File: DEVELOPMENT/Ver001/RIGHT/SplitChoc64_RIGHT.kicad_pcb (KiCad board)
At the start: 2 copper layers, 177.6 x 96.8 mm, 80 parts, among them J2 BM02B-SRSS-TB, J4 3V3 GND X Y SW SDA SCL, U2 XIAO nRF52840 Plus

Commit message: Stage parallel trackball FFC connectors in Ver001
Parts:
- added J6: FH19C-6S-0.5SH(10), SplitChoc64_FFC:FH19C-6S-0.5SH_HandSolder, B.Cu at (194.7, 112.0)
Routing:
- net R_GND: track 193.8 -> 198.8 mm, vias 2 -> 3
- net R_JOY_X: track 167.7 -> 172.4 mm, vias 1 -> 2
- net R_JOY_Y: track 170.1 -> 171.1 mm, vias 1 -> 2
- net R_3V3: track 157.5 -> 158.1 mm, vias 2 -> 3
- net R_JOY_SW: track 165.4 -> 165.9 mm, vias 1 -> 2
- net R_JOY_SDA: track 165.7 -> 166.0 mm, vias 1 -> 2

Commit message: Repair parallel FFC fanout and publish DRC pass 2
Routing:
- net R_3V3: track 158.1 -> 179.2 mm, vias 3 -> 2
- net R_JOY_Y: track 171.1 -> 182.5 mm, vias 2 -> 1
- net R_JOY_SW: track 165.9 -> 177.0 mm, vias 2 -> 1
- net R_JOY_SDA: track 166.0 -> 176.5 mm, vias 2 -> 1
- net R_GND: track 198.8 -> 207.7 mm, vias 3 -> 2
- net R_JOY_X: track 172.4 -> 180.9 mm, vias 2 -> 1
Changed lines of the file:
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@@
 	(segment
 		(start 198.95 115.05)
-		(end 198.0 110.0949)
+		(end 185.073 116.0)
 		(width 0.15)
 		(layer "B.Cu")
 		(net 14)
 	)
-	(via
-		(at 198.0 110.0949)
-		(size 0.45)
-		(drill 0.2)
-		(layers "F.Cu" "B.Cu")
-		(net 14)
-	)
 	(segment
 		(start 199.45 115.05)
-		(end 198.8 110.3966)
+		(end 186.343 116.0)
 		(width 0.15)
 		(layer "B.Cu")
 		(net 16)
 	)
-	(via
-		(at 198.8 110.3966)
-		(size 0.45)
-		(drill 0.2)
-		(layers "F.Cu" "B.Cu")
-		(net 16)
-	)
 	(segment
 		(start 199.95 115.05)
-		(end 199.8 114.3)
+		(end 187.613 116.0)
 		(width 0.15)
 		(layer "B.Cu")
 		(net 17)
 	)
-	(via
-		(at 199.8 114.3)
-		(size 0.45)
-		(drill 0.2)
-		(layers "F.Cu" "B.Cu")
-		(net 17)
-	)
 	(segment
 		(start 200.45 115.05)
-		(end 200.4 114.72)
+		(end 188.883 116.0)
 		(width 0.15)
 		(layer "B.Cu")
 		(net 18)
 	)
-	(via
-		(at 200.4 114.72)
-		(size 0.45)
-		(drill 0.2)
-		(layers "F.Cu" "B.Cu")
-		(net 18)
-	)
 	(segment
 		(start 200.95 115.05)
-		(end 201.0 114.98)
+		(end 190.153 116.0)
 		(width 0.15)
 		(layer "B.Cu")
 		(net 19)
 	)
-	(via
-		(at 201.0 114.98)
-		(size 0.45)
-		(drill 0.2)
-		(layers "F.Cu" "B.Cu")
-		(net 19)
-	)
 	(segment
 		(start 201.45 115.05)
-		(end 201.6 115.4)
+		(end 201.45 113.5)
 		(width 0.15)
 		(layer "B.Cu")
 		(net 21)
 	)
-	(via
-		(at 201.6 115.4)
-		(size 0.45)
-		(drill 0.2)
-		(layers "F.Cu" "B.Cu")
+	(segment
+		(start 201.45 113.5)
+		(end 183.803 113.5)
+		(width 0.15)
+		(layer "B.Cu")
 		(net 21)
 	)
 	(segment
-		(start 199.8 114.3)
-		(end 199.8 114.5693)
+		(start 183.803 113.5)
+		(end 183.803 116.0)
 		(width 0.15)
-		(layer "F.Cu")
-		(net 17)
-	)
-	(segment
-		(start 200.4 114.72)
-		(end 200.4 114.871)
-		(width 0.15)
-		(layer "F.Cu")
-		(net 18)
-	)
-	(segment
-		(start 201.0 114.98)
-		(end 201.0 115.1727)
-		(width 0.15)
-		(layer "F.Cu")
-		(net 19)
-	)
-	(segment
-		(start 201.6 115.4)
-		(end 201.6 115.6065)
-		(width 0.15)
-		(layer "F.Cu")
+		(layer "B.Cu")
 		(net 21)
 	)

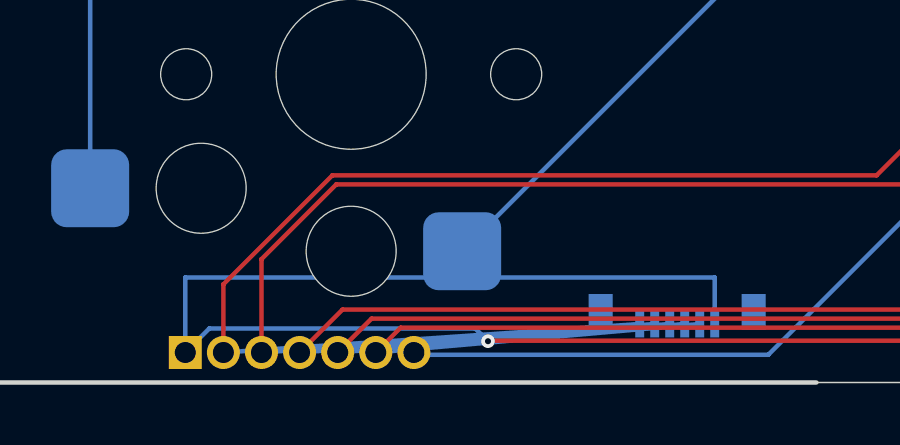
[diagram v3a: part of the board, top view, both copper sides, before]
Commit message: Rebuild clean Ver001 FFC footprint placement and DRC
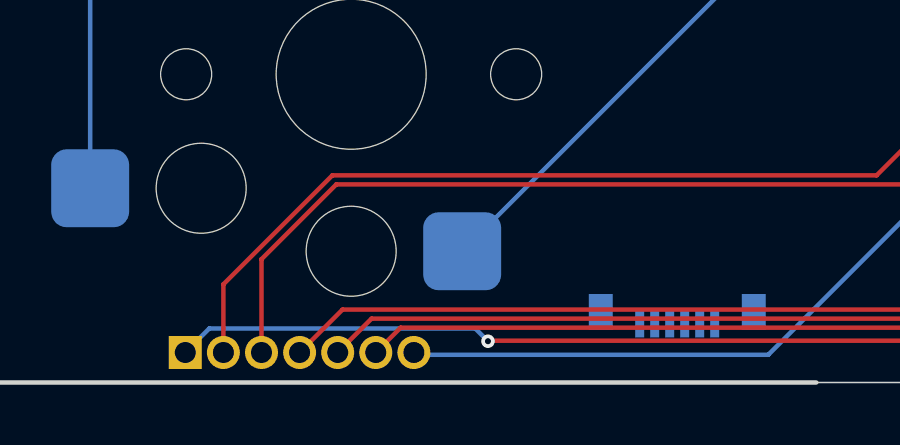
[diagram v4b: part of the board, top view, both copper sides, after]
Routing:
- net R_3V3: track 179.2 -> 157.5 mm
- net R_GND: track 207.7 -> 193.8 mm
- net R_JOY_X: track 180.9 -> 167.7 mm
- net R_JOY_Y: track 182.5 -> 170.1 mm
- net R_JOY_SW: track 177.0 -> 165.4 mm
- net R_JOY_SDA: track 176.5 -> 165.7 mm
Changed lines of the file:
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@@
 		(net 59)
-	)
-	(segment
-		(start 198.95 115.05)
-		(end 185.073 116.0)
-		(width 0.15)
-		(layer "B.Cu")
-		(net 14)
-	)
-	(segment
-		(start 199.45 115.05)
-		(end 186.343 116.0)
-		(width 0.15)
-		(layer "B.Cu")
-		(net 16)
-	)
-	(segment
-		(start 199.95 115.05)
-		(end 187.613 116.0)
-		(width 0.15)
-		(layer "B.Cu")
-		(net 17)
-	)
-	(segment
-		(start 200.45 115.05)
-		(end 188.883 116.0)
-		(width 0.15)
-		(layer "B.Cu")
-		(net 18)
-	)
-	(segment
-		(start 200.95 115.05)
-		(end 190.153 116.0)
-		(width 0.15)
-		(layer "B.Cu")
-		(net 19)
-	)
-	(segment
-		(start 201.45 115.05)
-		(end 201.45 113.5)
-		(width 0.15)
-		(layer "B.Cu")
-		(net 21)
-	)
-	(segment
-		(start 201.45 113.5)
-		(end 183.803 113.5)
-		(width 0.15)
-		(layer "B.Cu")
-		(net 21)
-	)
-	(segment
-		(start 183.803 113.5)
-		(end 183.803 116.0)
-		(width 0.15)
-		(layer "B.Cu")
-		(net 21)
 	)
 	(embedded_fonts no)

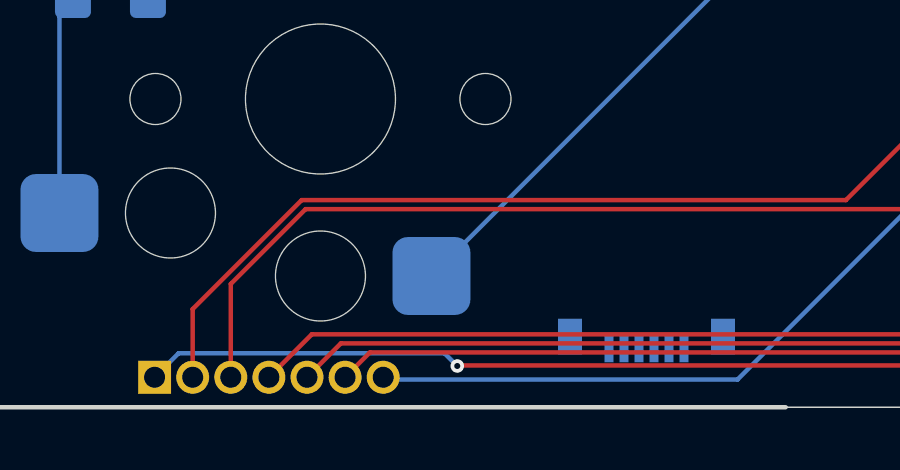
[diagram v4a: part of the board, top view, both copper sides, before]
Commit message: Route Ver001 FFC power nets and publish DRC
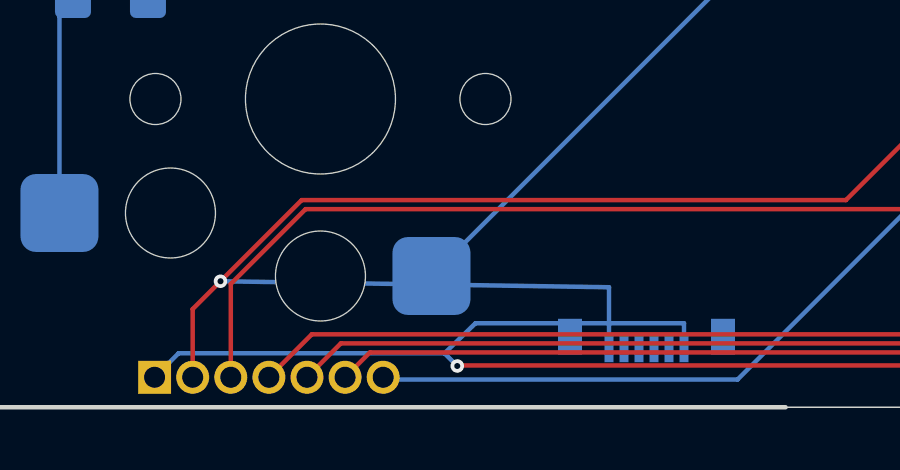
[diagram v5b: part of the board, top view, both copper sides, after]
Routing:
- net R_GND: track 193.8 -> 208.8 mm, vias 2 -> 3
- net R_3V3: track 157.5 -> 166.8 mm
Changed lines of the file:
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@@
 		(net 59)
+	)
+	(segment
+		(start 198.95 115.05)
+		(end 198.95 113.0)
+		(width 0.15)
+		(layer "B.Cu")
+		(net 14)
+	)
+	(segment
+		(start 198.95 113.0)
+		(end 186.0 112.7999)
+		(width 0.15)
+		(layer "B.Cu")
+		(net 14)
+	)
+	(via
+		(at 186.0 112.7999)
+		(size 0.45)
+		(drill 0.2)
+		(layers "F.Cu" "B.Cu")
+		(net 14)
+	)
+	(segment
+		(start 201.45 115.05)
+		(end 201.45 114.2)
+		(width 0.15)
+		(layer "B.Cu")
+		(net 21)
+	)
+	(segment
+		(start 201.45 114.2)
+		(end 194.5 114.2)
+		(width 0.15)
+		(layer "B.Cu")
+		(net 21)
+	)
+	(segment
+		(start 194.5 114.2)
+		(end 193.4677 115.2)
+		(width 0.15)
+		(layer "B.Cu")
+		(net 21)
 	)
 	(embedded_fonts no)

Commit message: Restore un-routed FFC footprints for Freerouting
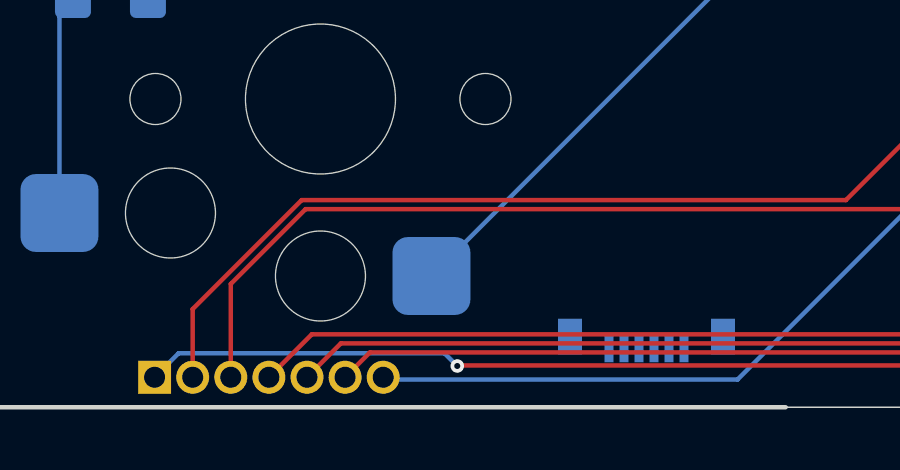
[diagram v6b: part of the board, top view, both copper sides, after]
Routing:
- net R_GND: track 208.8 -> 193.8 mm, vias 3 -> 2
- net R_3V3: track 166.8 -> 157.5 mm
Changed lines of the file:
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@@
 		(net 59)
-	)
-	(segment
-		(start 198.95 115.05)
-		(end 198.95 113.0)
-		(width 0.15)
-		(layer "B.Cu")
-		(net 14)
-	)
-	(segment
-		(start 198.95 113.0)
-		(end 186.0 112.7999)
-		(width 0.15)
-		(layer "B.Cu")
-		(net 14)
-	)
-	(via
-		(at 186.0 112.7999)
-		(size 0.45)
-		(drill 0.2)
-		(layers "F.Cu" "B.Cu")
-		(net 14)
-	)
-	(segment
-		(start 201.45 115.05)
-		(end 201.45 114.2)
-		(width 0.15)
-		(layer "B.Cu")
-		(net 21)
-	)
-	(segment
-		(start 201.45 114.2)
-		(end 194.5 114.2)
-		(width 0.15)
-		(layer "B.Cu")
-		(net 21)
-	)
-	(segment
-		(start 194.5 114.2)
-		(end 193.4677 115.2)
-		(width 0.15)
-		(layer "B.Cu")
-		(net 21)
 	)
 	(embedded_fonts no)
